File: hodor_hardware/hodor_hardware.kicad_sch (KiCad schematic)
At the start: 0 parts

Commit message: Schematic finished
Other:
- sheet Power & Terminals renamed Power
- sheet Controller ports: added ADC_CH1, ADC_CH2, ADC_CH3, ADC_CH4, DRV_EN, DRV_PWM1, DRV_PWM2, DRV_~{SF}, ENCODER_A, ENCODER_B, INPUT_1, INPUT_2, INPUT_3, INPUT_4, OUT_CTRL_1, OUT_CTRL_2, RELAY_CTRL_1, RELAY_CTRL_2, SAFETY_TRIG, SAFETY_~{CLR}; removed none
- sheet Peripherals ports: added OUT_CTRL_1, OUT_CTRL_2; removed none

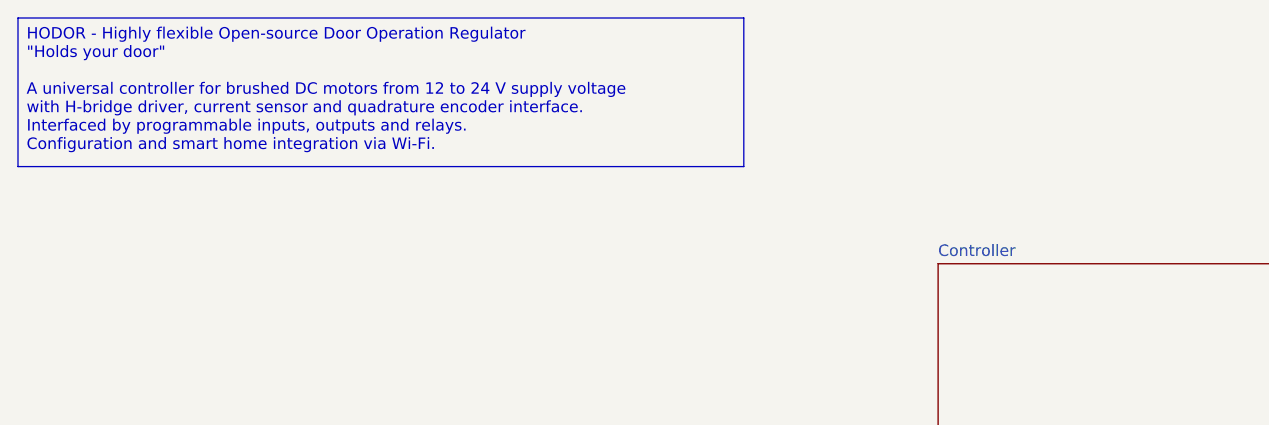
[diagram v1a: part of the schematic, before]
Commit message: Reworked into 2 PCBs
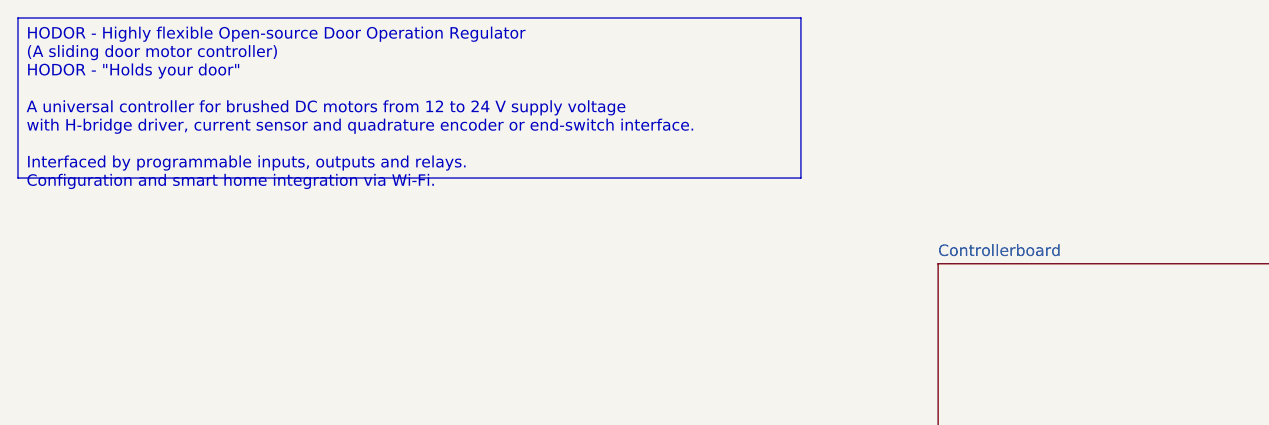
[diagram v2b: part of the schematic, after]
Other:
- sheet Controller renamed Controllerboard
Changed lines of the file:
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@@
 		(company "smartintech.de")
 	)
-	(text_box "HODOR - Highly flexible Open-source Door Operation Regulator\n\"Holds your door\"\n\nA universal controller for brushed DC motors from 12 to 24 V supply voltage\nwith H-bridge driver, current sensor and quadrature encoder interface. \nInterfaced by programmable inputs, outputs and relays.\nConfiguration and smart home integration via Wi-Fi."
+	(text_box "HODOR - Highly flexible Open-source Door Operation Regulator\n(A sliding door motor controller)\nHODOR - \"Holds your door\"\n\nA universal controller for brushed DC motors from 12 to 24 V supply voltage\nwith H-bridge driver, current sensor and quadrature encoder or end-switch interface. \nInterfaced by programmable inputs, outputs and relays.\nConfiguration and smart home integration via Wi-Fi."
 		(exclude_from_sim no)
 		(at 15.875 15.875 0)
-		(size 80.645 16.51)
+		(size 86.995 17.78)
 		(margins 0.9525 0.9525 0.9525 0.9525)
 		(stroke
@@
 			(color 0 0 0 0.0000)
 		)
-		(property "Sheetname" "Controller"
+		(property "Sheetname" "Controllerboard"
 			(at 118.11 42.4684 0)
 			(effects

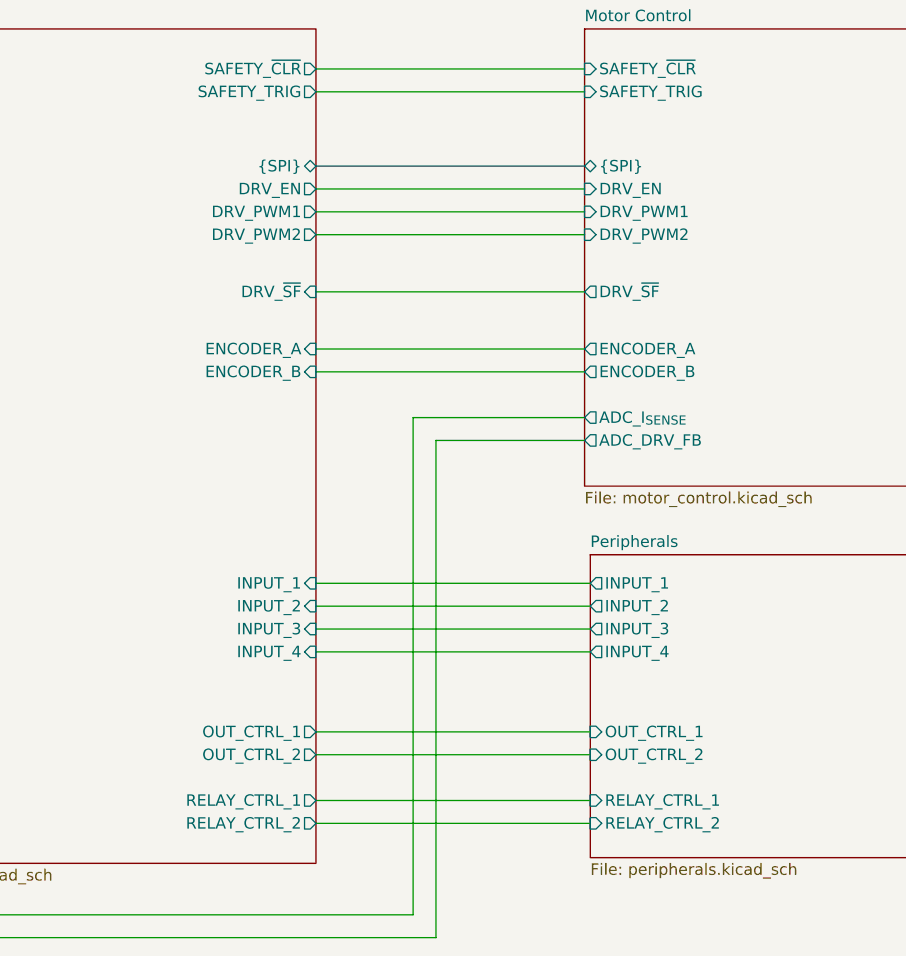
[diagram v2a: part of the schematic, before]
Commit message: Finished schematic - DRC ok.
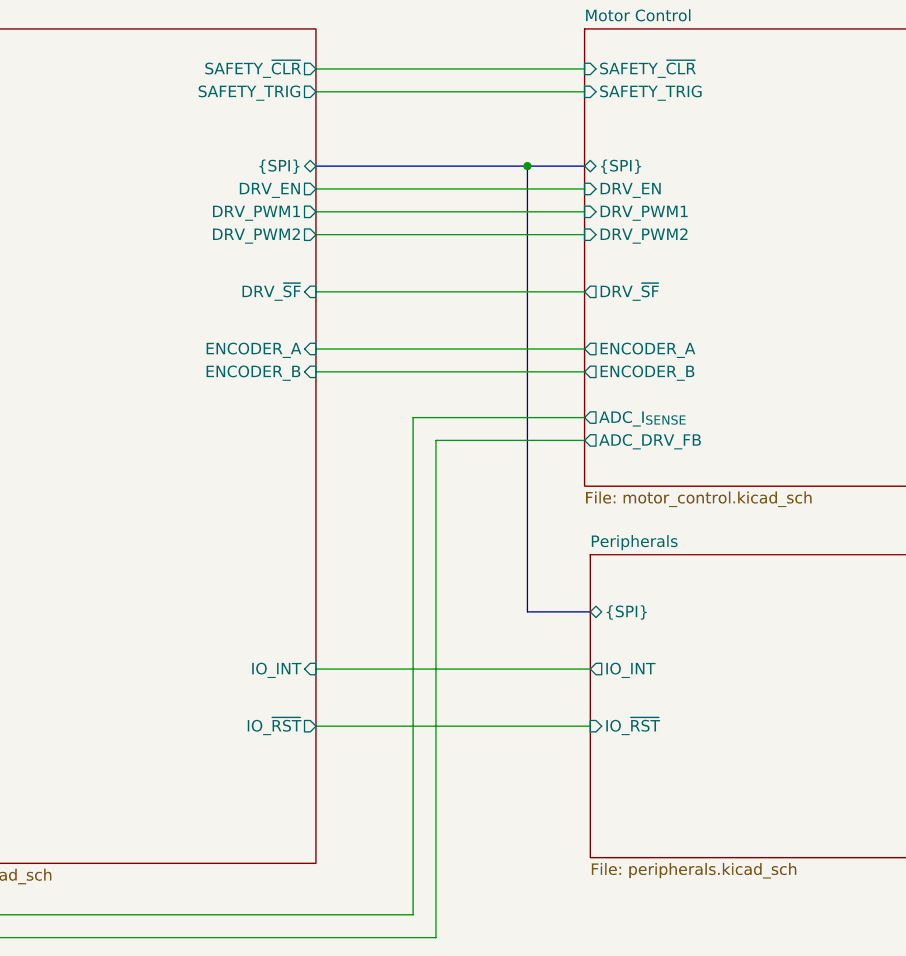
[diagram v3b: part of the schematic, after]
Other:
- sheet Controllerboard ports: added IO_INT, IO_~{RST}; removed INPUT_1, INPUT_2, INPUT_3, INPUT_4, OUT_CTRL_1, OUT_CTRL_2, RELAY_CTRL_1, RELAY_CTRL_2
- sheet Peripherals ports: added IO_INT, IO_~{RST}, {SPI}; removed INPUT_1, INPUT_2, INPUT_3, INPUT_4, OUT_CTRL_1, OUT_CTRL_2, RELAY_CTRL_1, RELAY_CTRL_2
